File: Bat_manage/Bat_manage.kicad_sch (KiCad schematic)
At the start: 7 parts, among them Q1 NMOS

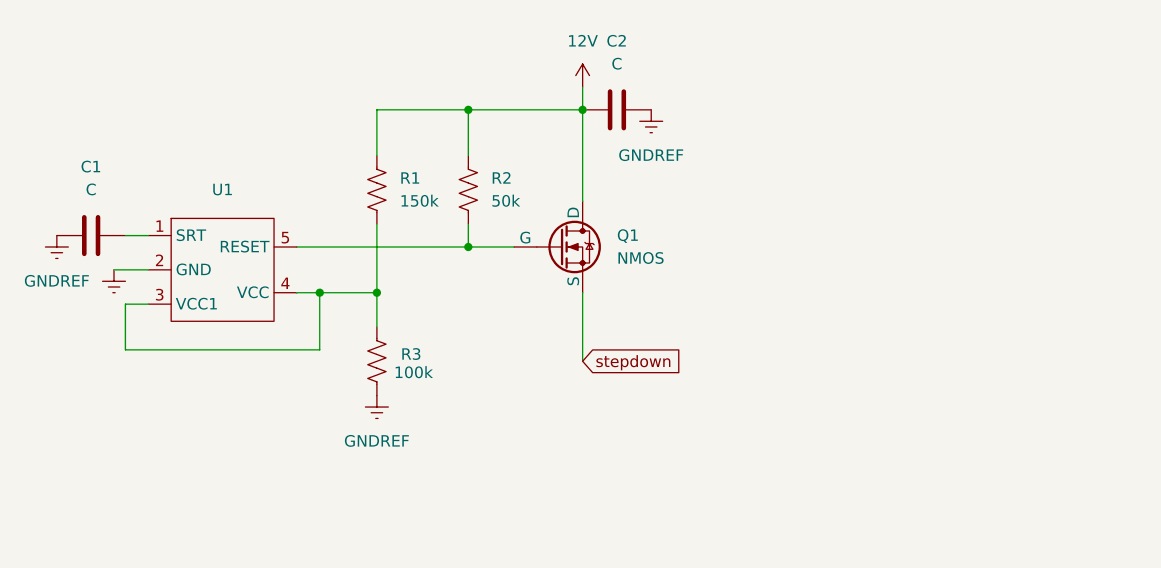
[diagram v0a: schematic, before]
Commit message: pushing battery management design with relay
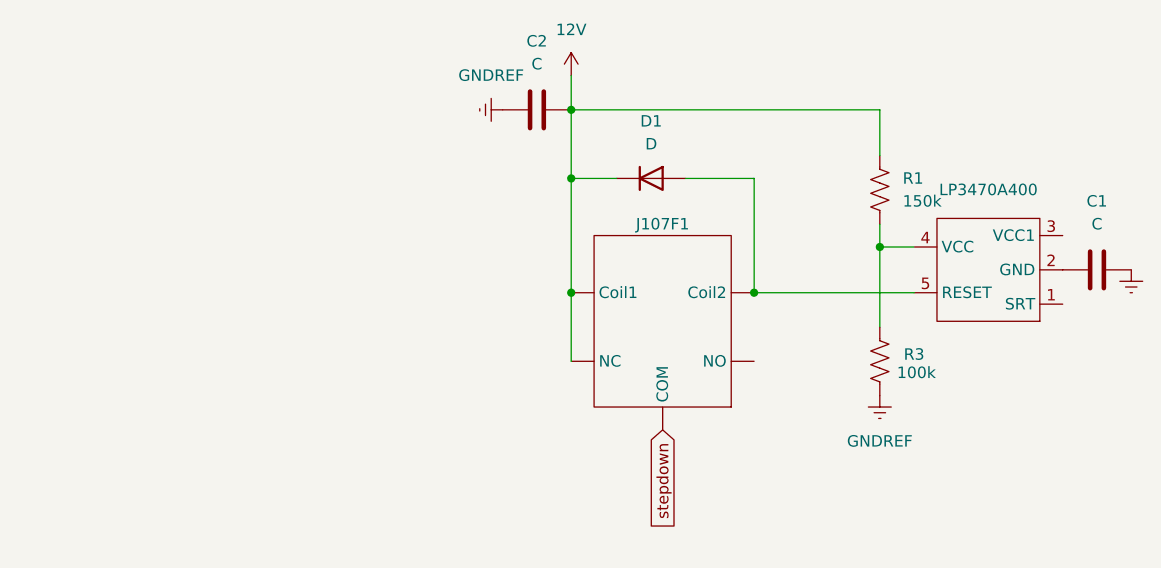
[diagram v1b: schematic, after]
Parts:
- removed Q1: NMOS, symbol Simulation_SPICE:NMOS
- removed R2: 50k, symbol Device:R_US
- added D1: D, symbol Device:D
- added J107F1: ~, symbol Bat_lib:J107F
- renumbered U1 to LP3470A400
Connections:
- net 12V: now also C2.2, D1.1 (K), J107F1. (NO); no longer C2.1
- net GNDREF: now also C1.2, C2.1; no longer C1.1, C2.2, LP3470A400.2 (GND)
- net stepdown: now also J107F1. (NO)
- net at LP3470A400.5 (RESET): now also D1.2 (A), J107F1. (NO)
- net at LP3470A400.1 (SRT): no longer C1.2
- net at LP3470A400.4 (VCC), R1.2, R3.1: no longer LP3470A400.3 (VCC1)
- new net: C1.1, LP3470A400.2 (GND)
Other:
- moved on the sheet: C2, LP3470A400, R1, R3
